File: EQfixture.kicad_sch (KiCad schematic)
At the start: 47 parts, among them J2 Conn_02x05_Top_Bottom, J3 Conn_01x06, J4 Conn_01x03, J4 Conn_02x10_Top_Bottom

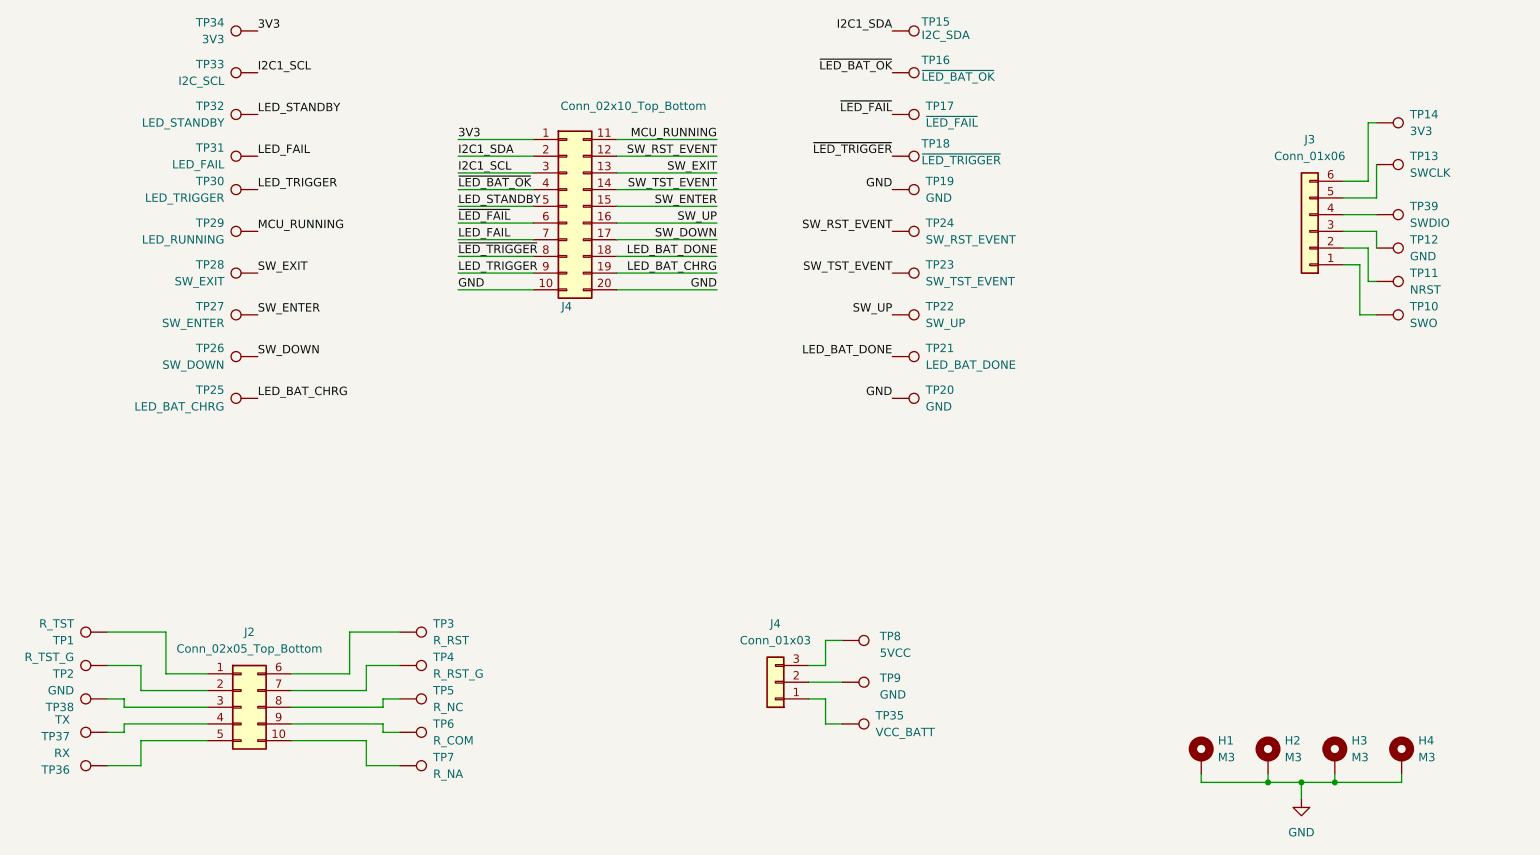
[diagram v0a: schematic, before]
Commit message: pogos added
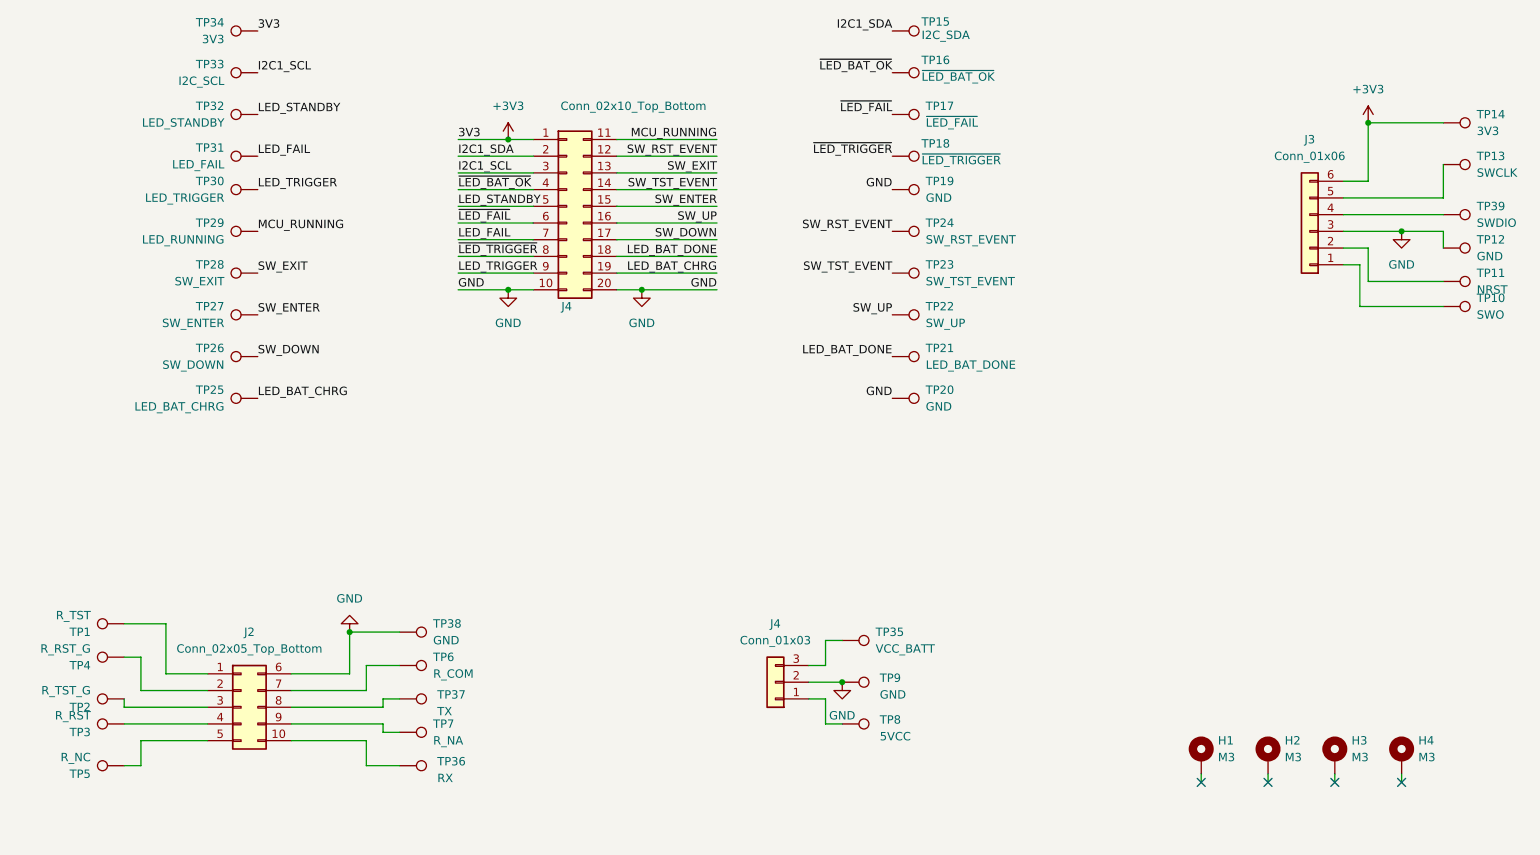
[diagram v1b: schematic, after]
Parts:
- J2: footprint (none) -> Connector_PinHeader_2.54mm:PinHeader_2x05_P2.54mm_Vertical
- J3: footprint (none) -> Connector_PinHeader_2.54mm:PinHeader_1x06_P2.54mm_Vertical
- J4: footprint (none) -> Connector_PinHeader_2.54mm:PinHeader_1x03_P2.54mm_Vertical
- J4: footprint Connector_IDC:IDC-Header_2x10_P2.54mm_Vertical -> Connector_PinHeader_2.54mm:PinHeader_2x10_P2.54mm_Vertical
- TP1, TP10, TP11, TP12, TP13, TP15, TP16, TP17, TP18, TP19, TP2, TP20, TP21, TP22, TP23, TP24, TP25, TP26, TP27, TP28, TP29, TP3, TP30, TP31, TP32, TP33, TP34, TP35, TP36, TP37, TP38, TP39, TP4, TP5, TP6, TP7, TP8, TP9: footprint (none) -> my_footprints:TestPoint-TH-Square-1mmHole
- TP14: footprint Connector_Pin:Pin_D1.0mm_L10.0mm -> my_footprints:TestPoint-TH-Square-1mmHole
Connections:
- net 3V3 is gone; now on net +3V3: J4.1 (Pin_1), TP34.1
- net GND: now also J2.6 (Pin_6), J3.3 (Pin_3), J4.2 (Pin_2), TP12.1, TP38.1, TP9.1; no longer H1.1, H2.1, H3.1, H4.1
- net at TP5.1: now also J2.5 (Pin_5); no longer J2.8 (Pin_8)
- net at TP35.1: now also J4.3 (Pin_3); no longer J4.1 (Pin_1)
- net at TP37.1: now also J2.8 (Pin_8); no longer J2.4 (Pin_4)
- net at J2.10 (Pin_10): now also TP36.1; no longer TP7.1
- net at J2.2 (Pin_2): now also TP4.1; no longer TP2.1
- net at J2.3 (Pin_3): now also TP2.1; no longer TP38.1
- net at TP3.1: now also J2.4 (Pin_4); no longer J2.6 (Pin_6)
- net at J2.7 (Pin_7): now also TP6.1; no longer TP4.1
- net at J2.9 (Pin_9): now also TP7.1; no longer TP6.1
- net at TP8.1: now also J4.1 (Pin_1); no longer J4.3 (Pin_3)
- net +3V3: now reaches J3.6 (Pin_6), TP14.1
- no-connect marks 0 -> 4
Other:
- moved on the sheet: TP1, TP10, TP11, TP12, TP13, TP14, TP2, TP3, TP35, TP36, TP37, TP38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

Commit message: done + gerber added
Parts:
- H1, H2, H3, H4: footprint MountingHole:MountingHole_3.2mm_M3_Pad_Via -> MountingHole:MountingHole_3.2mm_M3_Pad
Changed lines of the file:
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@@
       (effects (font (size 1.27 1.27)) (justify left))
     )
-    (property "Footprint" "MountingHole:MountingHole_3.2mm_M3_Pad_Via" (at 233.68 148.59 0)
+    (property "Footprint" "MountingHole:MountingHole_3.2mm_M3_Pad" (at 233.68 148.59 0)
       (effects (font (size 1.27 1.27)) hide)
     )
@@
       (effects (font (size 1.27 1.27)) (justify left))
     )
-    (property "Footprint" "MountingHole:MountingHole_3.2mm_M3_Pad_Via" (at 243.84 148.59 0)
+    (property "Footprint" "MountingHole:MountingHole_3.2mm_M3_Pad" (at 243.84 148.59 0)
       (effects (font (size 1.27 1.27)) hide)
     )
@@
       (effects (font (size 1.27 1.27)) (justify left))
     )
-    (property "Footprint" "MountingHole:MountingHole_3.2mm_M3_Pad_Via" (at 223.52 148.59 0)
+    (property "Footprint" "MountingHole:MountingHole_3.2mm_M3_Pad" (at 223.52 148.59 0)
       (effects (font (size 1.27 1.27)) hide)
     )
@@
       (effects (font (size 1.27 1.27)) (justify left))
     )
-    (property "Footprint" "MountingHole:MountingHole_3.2mm_M3_Pad_Via" (at 254 148.59 0)
-      (effects (font (size 1.27 1.27)) hide)
-    )
+    (property "Footprint" "MountingHole:MountingHole_3.2mm_M3_Pad" (at 254 148.59 0)
+      (effects (font (size 1.27 1.27)) hide)
+    )
